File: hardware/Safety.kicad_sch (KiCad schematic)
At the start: 1 part, among them K3 ALDP105W

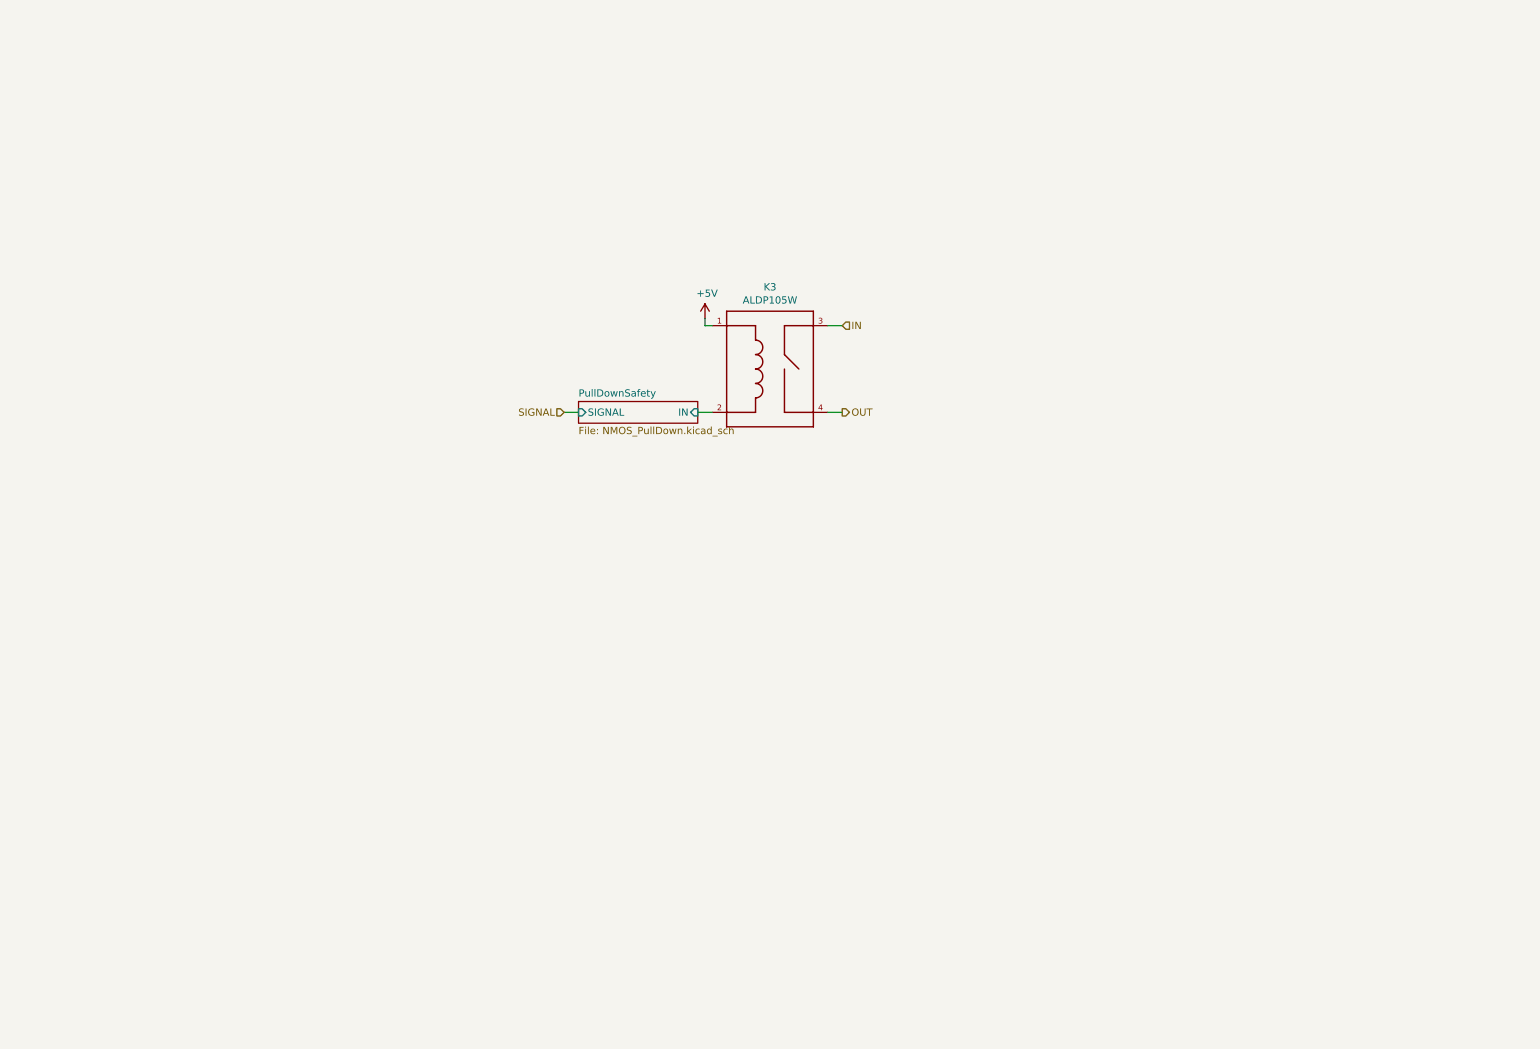
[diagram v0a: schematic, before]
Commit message: new firmware for bga version of stm, change stm from smt to bga, smaller HV dividers, added 3rd can transciver, and other
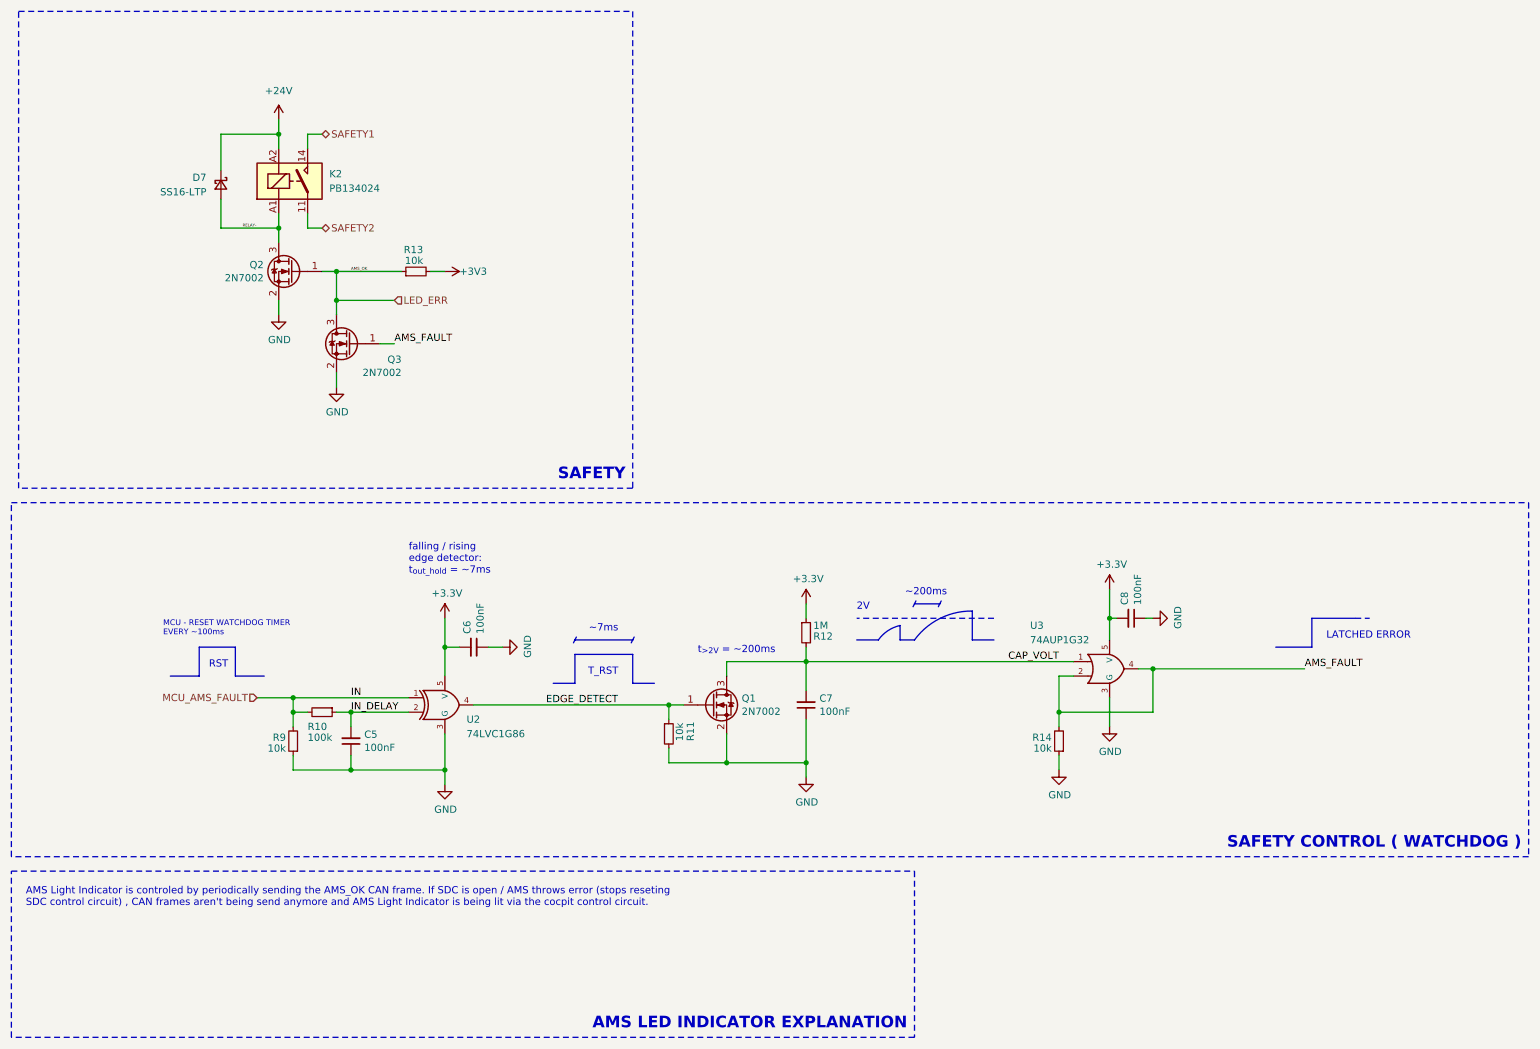
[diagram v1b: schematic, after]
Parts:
- removed K3: ALDP105W, RELAY_ALDP105W, symbol PUTM_EV_BMS_library:ALDP105W
- added C5, C6, C7, C8: 100nF, Capacitor_SMD:C_0603_1608Metric, symbol Device:C_Small
- added D7: SS16-LTP, Diode_SMD:D_SOD-123, symbol Device:D_Schottky_Small
- added K2: PB134024, Samacsys:PB134024, symbol Samacsys_kicad_sym:PB134024
- added Q1, Q2, Q3: 2N7002, Package_TO_SOT_SMD:SOT-23, symbol Transistor_FET:2N7002
- added R10: 100k, Resistor_SMD:R_0603_1608Metric, symbol Device:R_Small
- added R11, R13, R14, R9: 10k, Resistor_SMD:R_0603_1608Metric, symbol Device:R_Small
- added R12: 1M, Resistor_SMD:R_0603_1608Metric, symbol Device:R_Small
- added U2: 74LVC1G86, Package_TO_SOT_SMD:SOT-23-5, symbol 74xGxx:74LVC1G86
- added U3: 74AUP1G32, Package_TO_SOT_SMD:SOT-23-5, symbol 74xGxx:74AUP1G32
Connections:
- new net +24V: D7.1 (K), K2.A2 (COIL_2)
- new net +3.3V: C6.2, C8.2, R12.1, U2.5 (V), U3.5 (V)
- new net +3V3: R13.2
- new net AMS_FAULT: Q3.1 (G), R14.2, U3.2, U3.4
- new net CAP_VOLT: C7.2, Q1.3 (D), R12.2, U3.1
- new net EDGE_DETECT: Q1.1 (G), R11.1, U2.4
- new net GND: C5.1, C6.1, C7.1, C8.1, Q1.2 (S), Q2.2 (S), Q3.2 (S), R11.2, R14.1, R9.1, U2.3 (G), U3.3 (G)
- new net IN_DELAY: C5.2, R10.1, U2.2
- new net LED_ERR: Q2.1 (G), Q3.3 (D), R13.1
- new net MCU_AMS_FAULT: R10.2, R9.2, U2.1
- new net RELAY-: D7.2 (A), K2.A1 (COIL_1), Q2.3 (D)
- new net SAFETY1: K2.14 (NO)
- new net SAFETY2: K2.11 (COM)
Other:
- removed sheet PullDownSafety
- note added: "2V"
- note added: "AMS LED INDICATOR EXPLANATION"
- note added: "AMS Light Indicator is controled by periodically sending the AMS_OK CAN frame. If SDC is open / AMS throws error (stops reseting SDC control circuit) , CAN frames aren't being send anymore and AMS Light Indicator is being lit via the cocpit control circuit."
- note added: "LATCHED ERROR"
- note added: "MCU - RESET WATCHDOG TIMER EVERY ~100ms"
- note added: "RST"
- note added: "SAFETY"
- note added: "SAFETY CONTROL ( WATCHDOG )"
- note added: "T_RST"
- note added: "falling / rising edge detector: t_{out_hold} = ~7ms"
- note added: "t_{>2V} = ~200ms"
- note added: "~200ms"
- note added: "~7ms"
- title: (none) -> AMS

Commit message: mcu pinout done
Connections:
- net AMS_FAULT renamed WTDG_ERROR
- net MCU_AMS_FAULT renamed AMS_ERROR
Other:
- moved on the sheet: Q3
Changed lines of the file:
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@@
 	(wire
 		(pts
-			(xy 72.39 68.58) (xy 72.39 66.04)
+			(xy 72.39 71.12) (xy 72.39 66.04)
 		)
 		(stroke
@@
 	(wire
 		(pts
-			(xy 80.01 73.66) (xy 82.55 73.66)
+			(xy 80.01 76.2) (xy 82.55 76.2)
 		)
 		(stroke
@@
 	(wire
 		(pts
-			(xy 72.39 78.74) (xy 72.39 81.28)
+			(xy 72.39 81.28) (xy 72.39 83.82)
 		)
 		(stroke
@@
 		)
 	)
-	(label "AMS_FAULT"
-		(at 242.57 130.81 0)
-		(fields_autoplaced yes)
-		(effects
-			(font
-				(size 1.27 1.27)
-			)
-			(justify left bottom)
-		)
-	)
-	(label "AMS_FAULT"
-		(at 82.55 73.66 0)
-		(fields_autoplaced yes)
-		(effects
-			(font
-				(size 1.27 1.27)
-			)
-			(justify left bottom)
-		)
-	)
 	(label "EDGE_DETECT"
 		(at 109.22 137.16 0)
@@
 			)
 			(justify right bottom)
+		)
+	)
+	(hierarchical_label "WTDG_ERROR"
+		(shape output)
+		(at 242.57 130.81 0)
+		(fields_autoplaced yes)
+		(effects
+			(font
+				(size 1.27 1.27)
+			)
+			(justify left)
 		)
 	)
@@
 		)
 	)
-	(hierarchical_label "MCU_AMS_FAULT"
+	(hierarchical_label "AMS_ERROR"
 		(shape input)
 		(at 58.42 135.89 180)
@@
 		(shape bidirectional)
 		(at 69.85 53.34 0)
+		(fields_autoplaced yes)
+		(effects
+			(font
+				(size 1.27 1.27)
+			)
+			(justify left)
+		)
+	)
+	(hierarchical_label "WTDG_ERROR"
+		(shape output)
+		(at 82.55 76.2 0)
 		(fields_autoplaced yes)
 		(effects
@@
 		(lib_name "GND_5")
 		(lib_id "power:GND")
-		(at 72.39 81.28 0)
+		(at 72.39 83.82 0)
 		(unit 1)
 		(exclude_from_sim no)
@@
 		(dnp no)
 		(property "Reference" "#PWR046"
-			(at 72.39 87.63 0)
+			(at 72.39 90.17 0)
 			(effects
 				(font
@@
 		)
 		(property "Value" "GND"
-			(at 72.517 85.6742 0)
+			(at 72.517 88.2142 0)
 			(effects
 				(font
@@
 		)
 		(property "Footprint" ""
-			(at 72.39 81.28 0)
+			(at 72.39 83.82 0)
 			(effects
 				(font
@@
 		)
 		(property "Datasheet" ""
-			(at 72.39 81.28 0)
+			(at 72.39 83.82 0)
 			(effects
 				(font
@@
 		)
 		(property "Description" ""
-			(at 72.39 81.28 0)
+			(at 72.39 83.82 0)
 			(effects
 				(font
@@
 	(symbol
 		(lib_id "Transistor_FET:2N7002")
-		(at 74.93 73.66 0)
+		(at 74.93 76.2 0)
 		(mirror y)
 		(unit 1)
@@
 		(dnp no)
 		(property "Reference" "Q3"
-			(at 83.82 76.4286 0)
+			(at 83.82 78.9686 0)
 			(effects
 				(font
@@
 		)
 		(property "Value" "2N7002"
-			(at 83.82 78.74 0)
+			(at 83.82 81.28 0)
 			(effects
 				(font
@@
 		)
 		(property "Footprint" "Package_TO_SOT_SMD:SOT-23"
-			(at 69.85 75.565 0)
+			(at 69.85 78.105 0)
 			(effects
 				(font
@@
 		)
 		(property "Datasheet" "https://www.onsemi.com/pub/Collateral/NDS7002A-D.PDF"
-			(at 74.93 73.66 0)
+			(at 74.93 76.2 0)
 			(effects
 				(font
@@
 		)
 		(property "Description" ""
-			(at 74.93 73.66 0)
+			(at 74.93 76.2 0)
 			(effects
 				(font
@@
 		)
 		(property "Manufacturer_Name" "--"
-			(at 74.93 73.66 0)
+			(at 74.93 76.2 0)
 			(effects
 				(font
@@
 		)
 		(property "Manufacturer_Part_Number" "--"
-			(at 74.93 73.66 0)
+			(at 74.93 76.2 0)
 			(effects
 				(font
@@
 		)
 		(property "Arrow Part Number" ""
-			(at 74.93 73.66 0)
+			(at 74.93 76.2 0)
 			(effects
 				(font
@@
 		)
 		(property "Arrow Price/Stock" ""
-			(at 74.93 73.66 0)
+			(at 74.93 76.2 0)
 			(effects
 				(font
@@
 		)
 		(property "Mouser Url" ""
-			(at 74.93 73.66 0)
-			(effects
-				(font
+			(at 74.93 76.2 0)
+			(effects
+				(font

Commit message: mama comit
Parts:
- removed C5, C6: 100nF, Capacitor_SMD:C_0603_1608Metric, symbol Device:C_Small
- removed Q1, Q2, Q3: 2N7002, Package_TO_SOT_SMD:SOT-23, symbol Transistor_FET:2N7002
- removed R10: 100k, Resistor_SMD:R_0603_1608Metric, symbol Device:R_Small
- removed R9: 10k, Resistor_SMD:R_0603_1608Metric, symbol Device:R_Small
- removed U2: 74LVC1G86, Package_TO_SOT_SMD:SOT-23-5, symbol 74xGxx:74LVC1G86
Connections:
- net EDGE_DETECT is gone; now on net AMS_ERROR: R11.1
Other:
- note added: "ERR"
- note added: "MCU - DISCHARGE CAP"
- note added: "OK"
- note added: "SAFETY CONTROL"
- note removed: "MCU - RESET WATCHDOG TIMER EVERY ~100ms"
- note removed: "RST"
- note removed: "SAFETY CONTROL ( WATCHDOG )"
- note removed: "T_RST"
- note removed: "falling / rising edge detector: t_{out_hold} = ~7ms"
- note removed: "~7ms"
- moved on the sheet: C7, C8, R11, R12, R14, U3

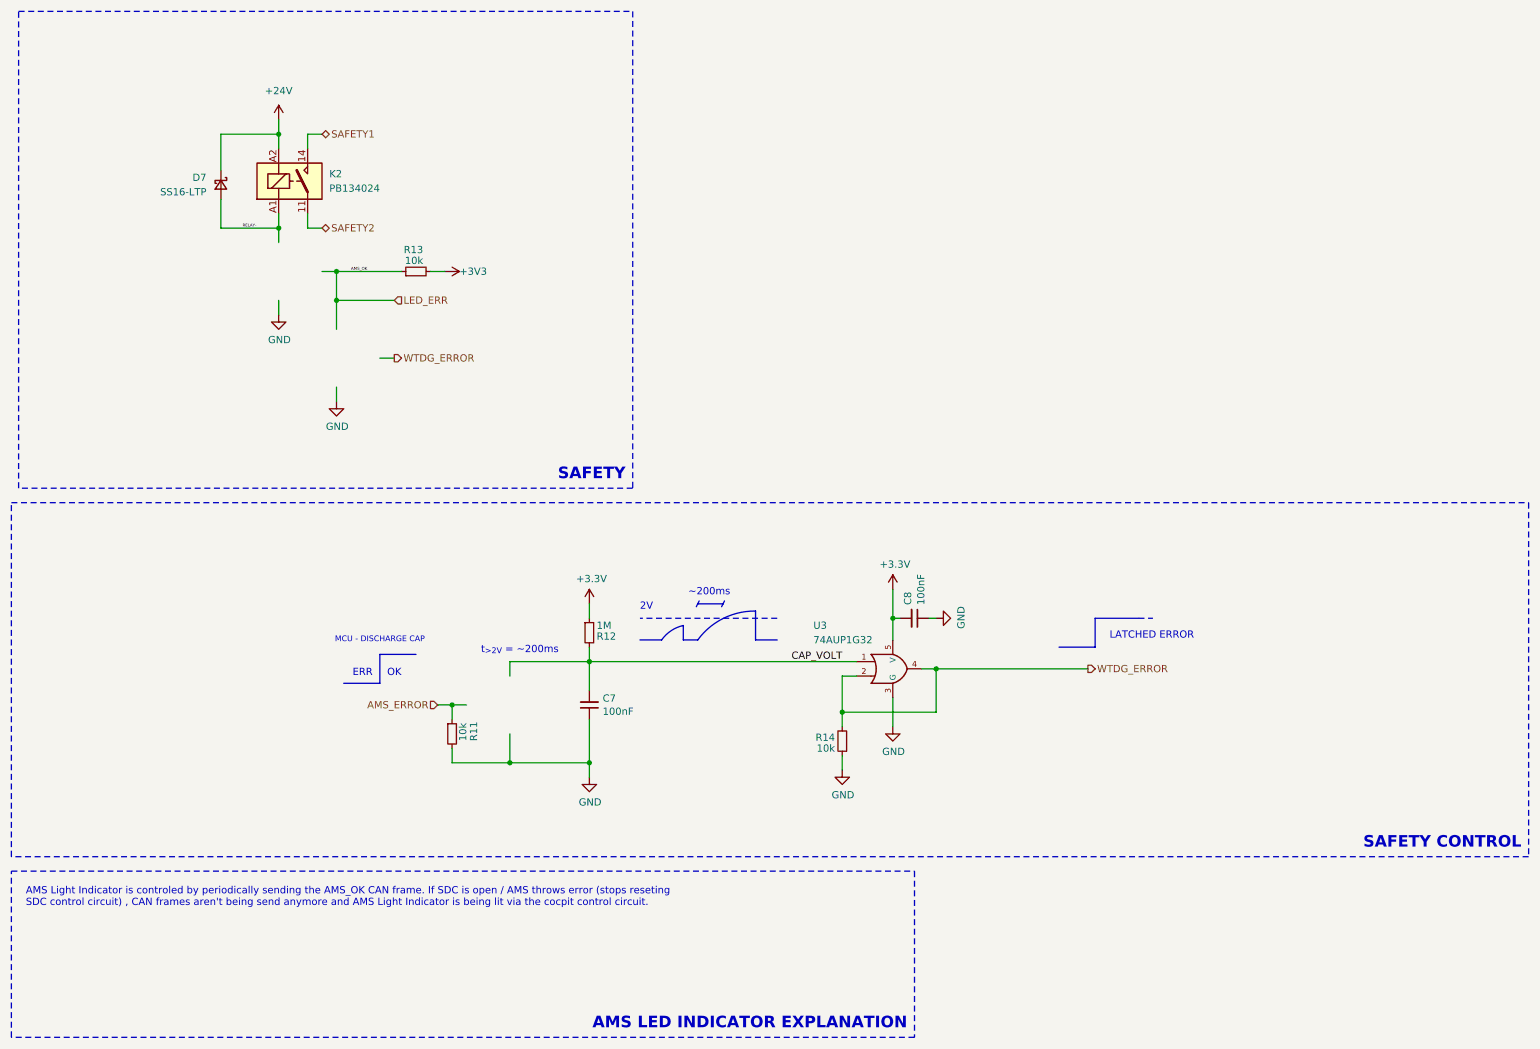
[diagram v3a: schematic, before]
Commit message: inductors 3d models fix, smaller relay (same series as the one from IMD), other + sync
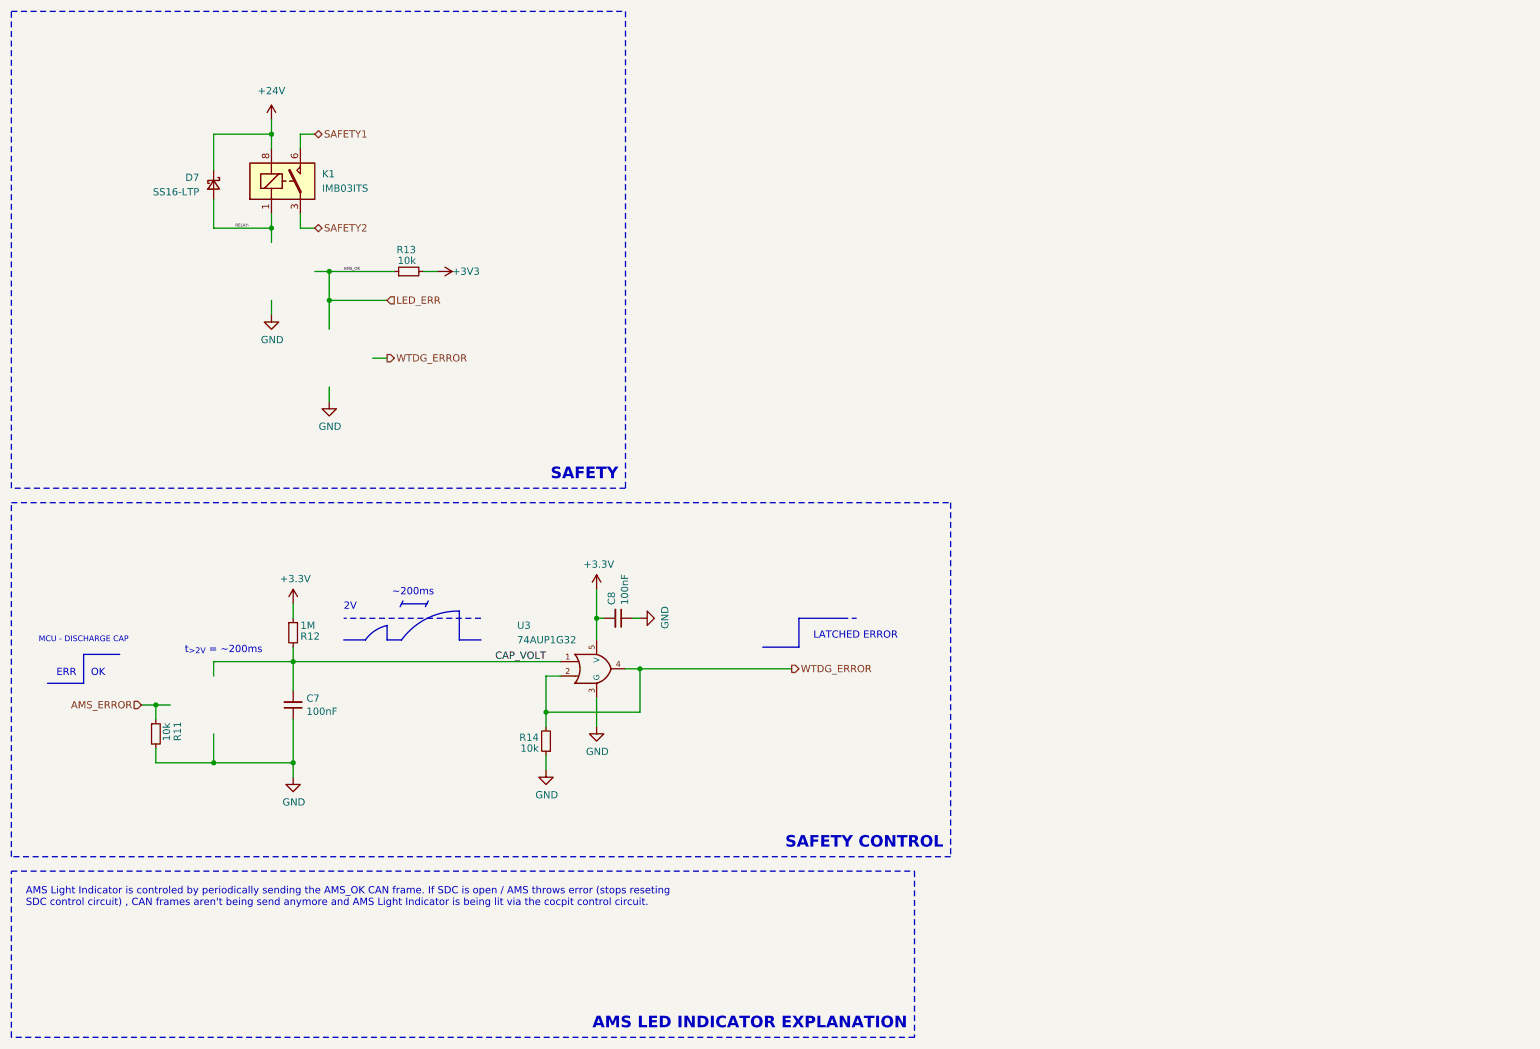
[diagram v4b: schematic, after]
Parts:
- removed K2: PB134024, Samacsys:PB134024, symbol Samacsys_kicad_sym:PB134024
- added K1: IMB03ITS, Samacsys:IMB03ITS, symbol Samacsys_kicad_sym:IMB03ITS
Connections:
- net +24V: now also K1.8 (COIL_2)
- net RELAY-: now also K1.1 (COIL_1)
- net SAFETY1: now also K1.6 (NO)
- net SAFETY2: now also K1.3 (COM)
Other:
- moved on the sheet: C7, C8, D7, R11, R12, R13, R14, U3
